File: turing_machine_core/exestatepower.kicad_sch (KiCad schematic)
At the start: 23 parts, among them J1 External Interface, U1 74LS04, U14 74LS74, U4 74LS00, U8 74LS30

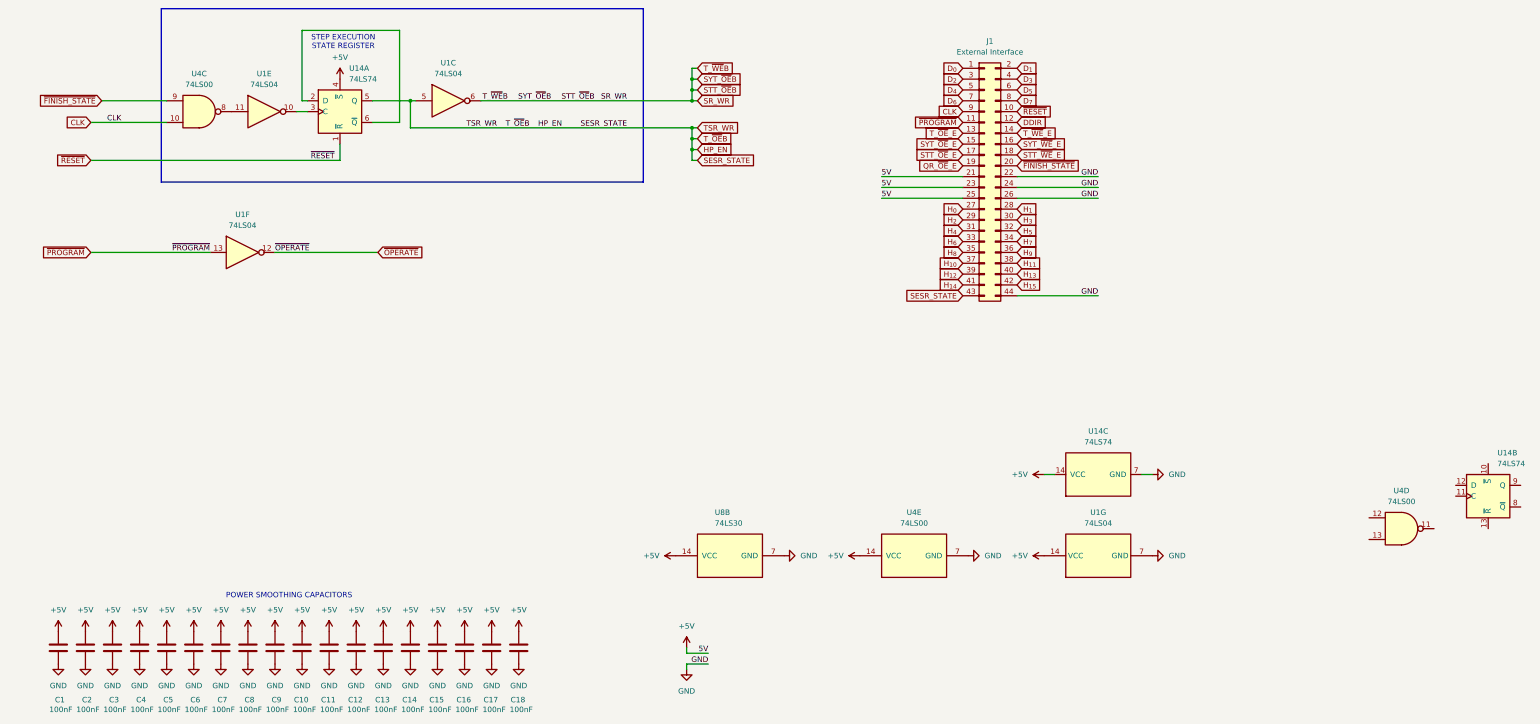
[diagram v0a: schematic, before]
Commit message: PCB layout planning and further documantation work
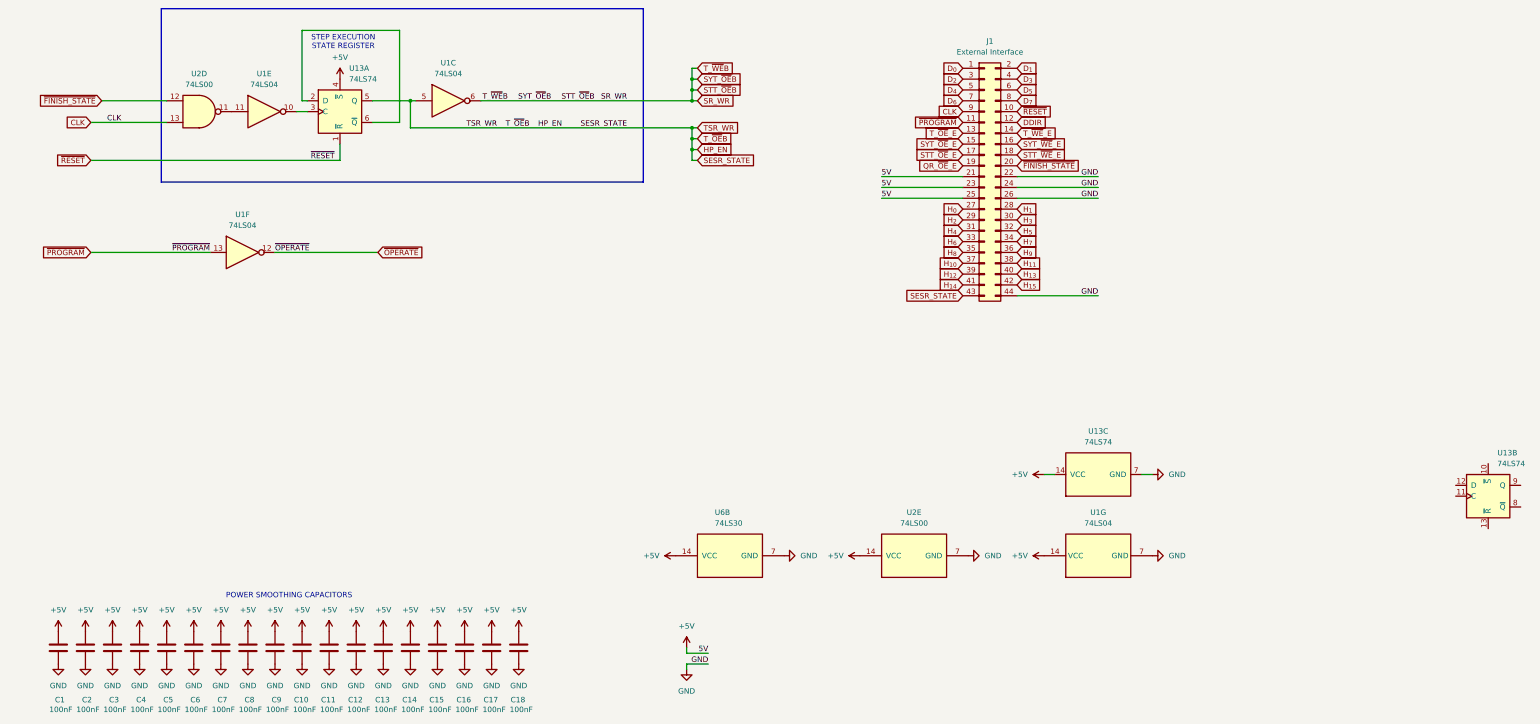
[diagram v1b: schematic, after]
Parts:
- removed U4: 74LS00, symbol 74xx:74LS00
- added U2: 74LS00, Package_DIP:DIP-14_W7.62mm, symbol 74xx:74LS00
- U1: footprint (none) -> Package_DIP:DIP-14_W7.62mm
- U13: renamed from U14; footprint (none) -> Package_DIP:DIP-14_W7.62mm
- U6: renamed from U8; footprint (none) -> Package_DIP:DIP-14_W7.62mm
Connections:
- net +5V: now also U2.14 (VCC)
- net CLK: now also U2.13
- net GND: now also U2.7 (GND)
- net ~{FINISH_STATE}: now also U2.12
- net at U1.11: now also U2.11

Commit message: finished PCB planning
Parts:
- added D1: Power LED, LED_THT:LED_D5.0mm, symbol Device:LED
- added R1: 1kΩ, Resistor_THT:R_Axial_DIN0207_L6.3mm_D2.5mm_P10.16mm_Horizontal, symbol Device:R
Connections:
- net +5V: now also U13.10 (~{S}), D1.2 (A)
- net GND: now also U13.11 (C), U13.12 (D), U13.13 (~{R}), R1.1
- new net: D1.1 (K), R1.2
- no-connect marks 0 -> 2
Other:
- moved on the sheet: U13B

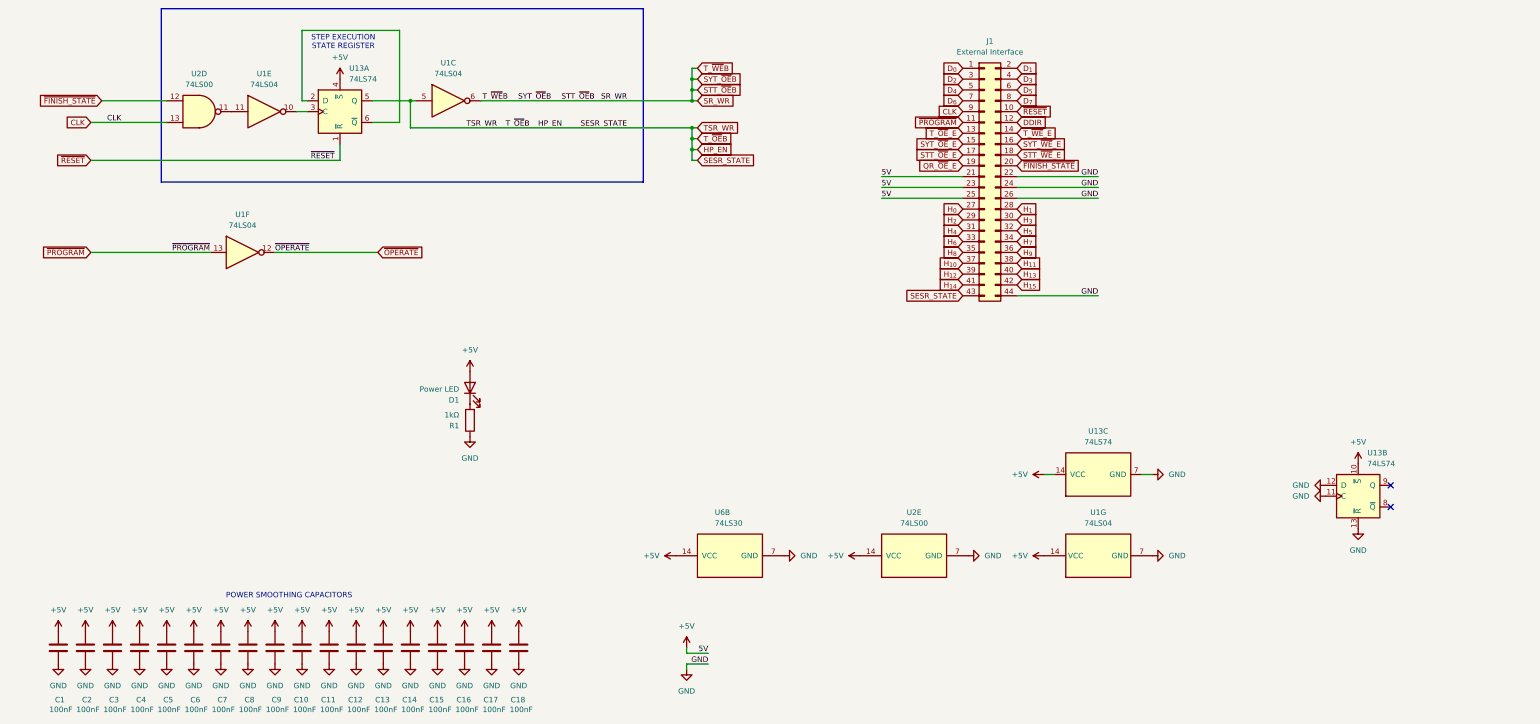
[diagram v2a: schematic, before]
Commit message: fixed schematics bugs and updated documentation
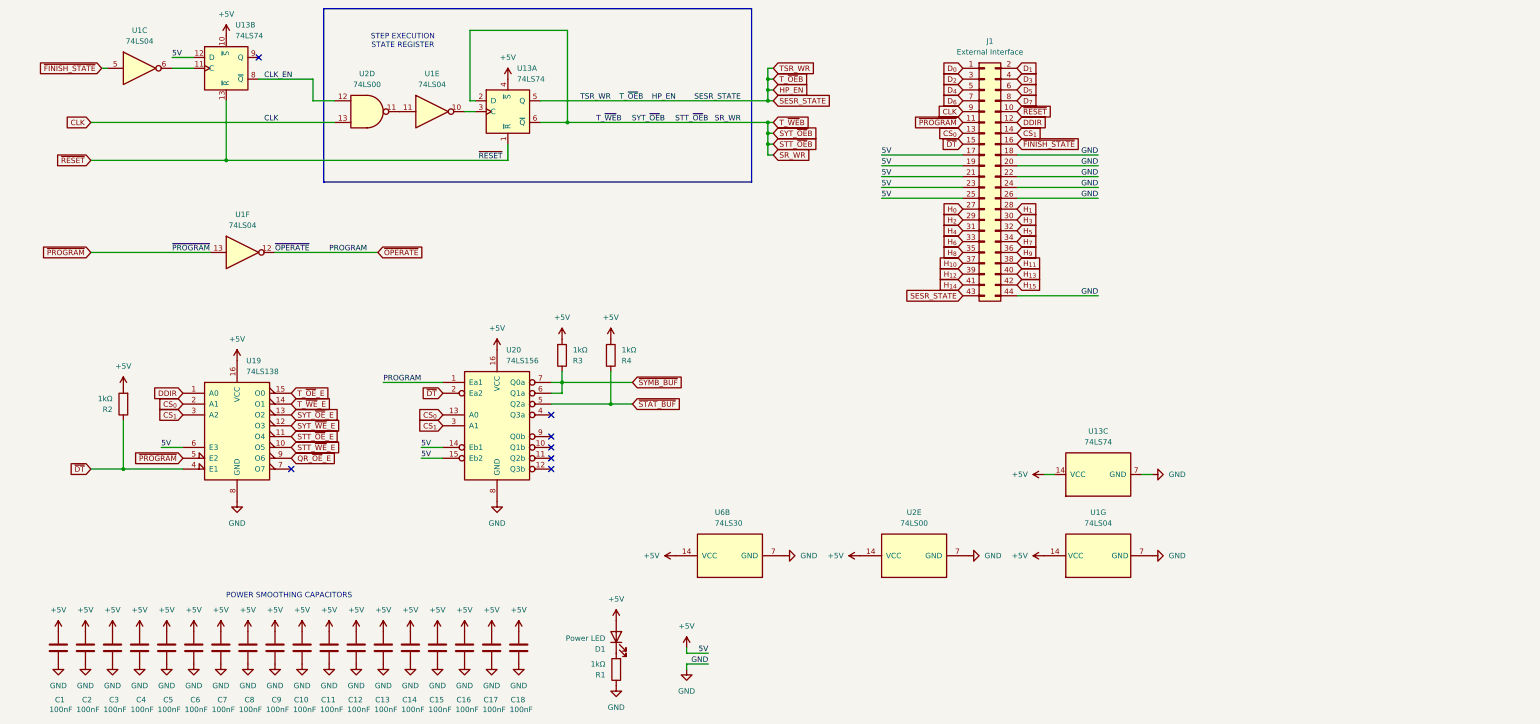
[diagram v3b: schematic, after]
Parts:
- added R2, R3, R4: 1kΩ, Resistor_THT:R_Axial_DIN0207_L6.3mm_D2.5mm_P10.16mm_Horizontal, symbol Device:R
- added U19: 74LS138, Package_DIP:DIP-16_W7.62mm, symbol 74xx:74LS138
- added U20: 74LS156, Package_DIP:DIP-16_W7.62mm, symbol 74xx:74LS156
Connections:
- net +5V: now also J1.17 (Pin_17), J1.19 (Pin_19), U13.12 (D), R2.2, R3.2, R4.2, U19.16 (VCC), U19.6 (E3), U20.14 (Eb1), U20.15 (Eb2), U20.16 (VCC)
- net DDIR: now also U19.1 (A0)
- net GND: now also J1.18 (Pin_18), J1.20 (Pin_20), U19.8 (GND), U20.8 (GND); no longer U13.11 (C), U13.12 (D), U13.13 (~{R})
- net HP_EN: no longer U1.5
- net QR_~{OE}_E: now also U19.9 (O6); no longer J1.19 (Pin_19)
- net SR_WR: now also U13.2 (D), U13.6 (~{Q}); no longer U1.6
- net STT_~{OE}_E: now also U19.11 (O4); no longer J1.17 (Pin_17)
- net STT_~{WE}_E: now also U19.10 (O5); no longer J1.18 (Pin_18)
- net SYT_~{OE}_E: now also U19.13 (O2); no longer J1.15 (Pin_15)
- net SYT_~{WE}_E: now also U19.12 (O3); no longer J1.16 (Pin_16)
- net T_~{OE}_E: now also U19.15 (O0); no longer J1.13 (Pin_13)
- net T_~{WE}_E: now also U19.14 (O1); no longer J1.14 (Pin_14)
- net ~{FINISH_STATE}: now also J1.16 (Pin_16), U1.5; no longer J1.20 (Pin_20), U2.12
- net ~{OPERATE}: now also U20.1 (Ea1)
- net ~{PROGRAM}: now also U19.5 (E2)
- net ~{RESET}: now also U13.13 (~{R})
- net CLK_EN: now reaches U13.8 (~{Q})
- net CLK_EN: now also U2.12
- new net: U1.6, U13.11 (C)
- new net CS_{0}: J1.13 (Pin_13), U19.2 (A1), U20.13 (A0)
- new net CS_{1}: J1.14 (Pin_14), U19.3 (A2), U20.3 (A1)
- new net ~{DT}: J1.15 (Pin_15), R2.1, U19.4 (E1), U20.2 (Ea2)
- new net ~{STAT_BUF}: R4.1, U20.5 (Q2a)
- new net ~{SYMB_BUF}: R3.1, U20.6 (Q1a), U20.7 (Q0a)
- no-connect marks 2 -> 7
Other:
- moved on the sheet: D1, R1, U13A, U13B, U1C, U1E, U2D

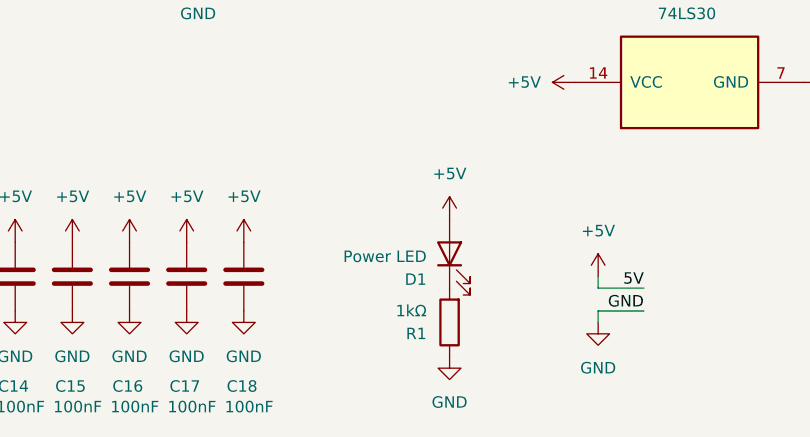
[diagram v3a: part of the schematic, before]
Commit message: adjusted PCB design for schematic fixes
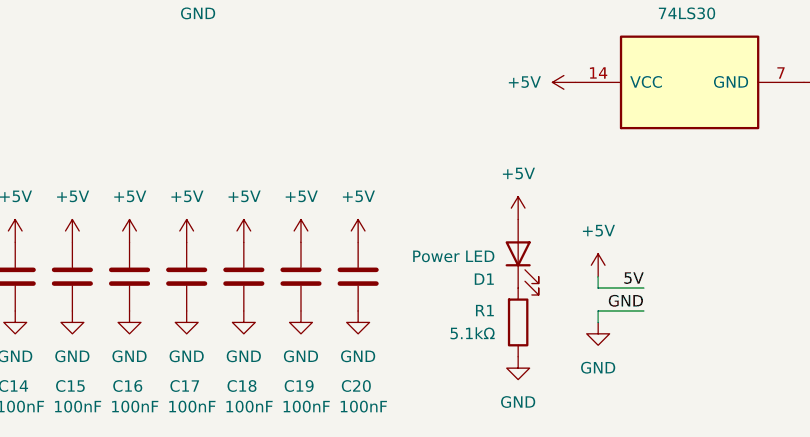
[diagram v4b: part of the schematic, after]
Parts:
- added C19, C20: 100nF, Capacitor_THT:C_Disc_D3.8mm_W2.6mm_P2.50mm, symbol Device:C
- R1: value 1kΩ -> 5.1kΩ
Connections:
- net +5V: now also C19.1, C20.1
- net GND: now also C19.2, C20.2
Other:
- moved on the sheet: D1, R1

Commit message: added edge connector to PCB
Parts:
- J1: footprint (none) -> Connector_Edge:Connector_Edge_2x22pin_odd
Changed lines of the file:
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@@
 			)
 		)
-		(property "Footprint" ""
+		(property "Footprint" "Connector_Edge:Connector_Edge_2x22pin_odd"
 			(at 234.95 69.85 0)
 			(effects

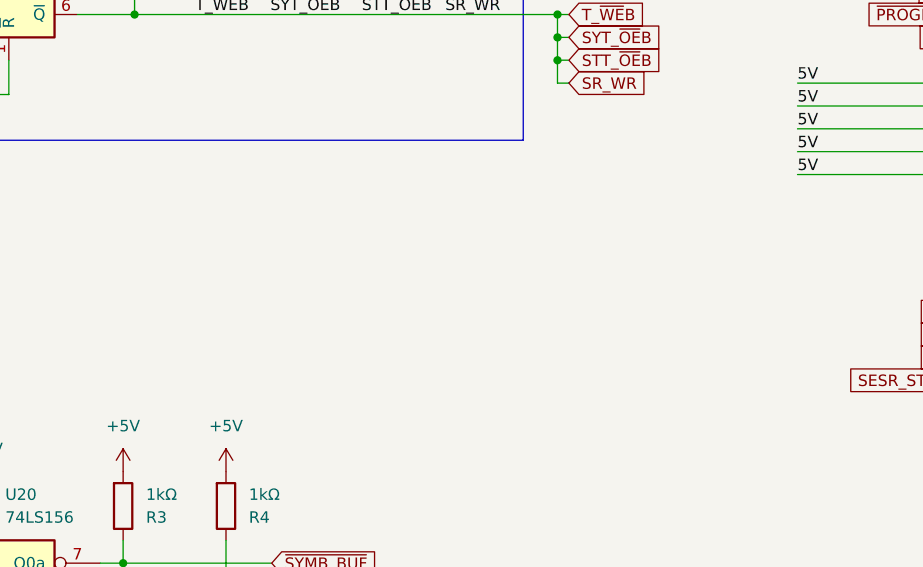
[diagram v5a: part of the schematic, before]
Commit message: added two connectors to schematics and PCB design and reformatted slightly documentation
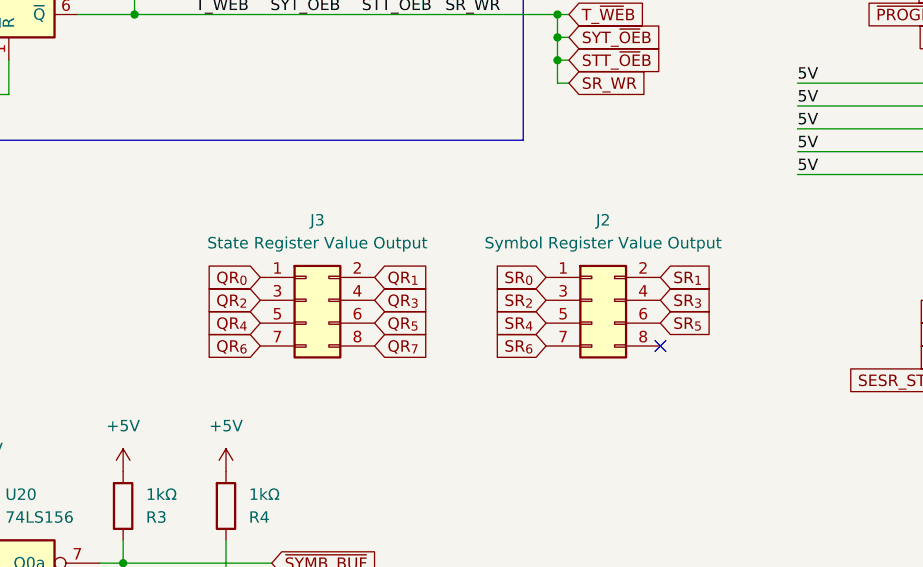
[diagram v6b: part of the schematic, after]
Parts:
- added J2: Symbol Register Value Output, Connector_PinHeader_2.54mm:PinHeader_2x04_P2.54mm_Vertical, symbol Connector_Generic:Conn_02x04_Odd_Even
- added J3: State Register Value Output, Connector_PinHeader_2.54mm:PinHeader_2x04_P2.54mm_Vertical, symbol Connector_Generic:Conn_02x04_Odd_Even
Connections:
- new net QR_{0}: J3.1 (Pin_1)
- new net QR_{1}: J3.2 (Pin_2)
- new net QR_{2}: J3.3 (Pin_3)
- new net QR_{3}: J3.4 (Pin_4)
- new net QR_{4}: J3.5 (Pin_5)
- new net QR_{5}: J3.6 (Pin_6)
- new net QR_{6}: J3.7 (Pin_7)
- new net QR_{7}: J3.8 (Pin_8)
- new net SR_{0}: J2.1 (Pin_1)
- new net SR_{1}: J2.2 (Pin_2)
- new net SR_{2}: J2.3 (Pin_3)
- new net SR_{3}: J2.4 (Pin_4)
- new net SR_{4}: J2.5 (Pin_5)
- new net SR_{5}: J2.6 (Pin_6)
- new net SR_{6}: J2.7 (Pin_7)
- no-connect marks 7 -> 8

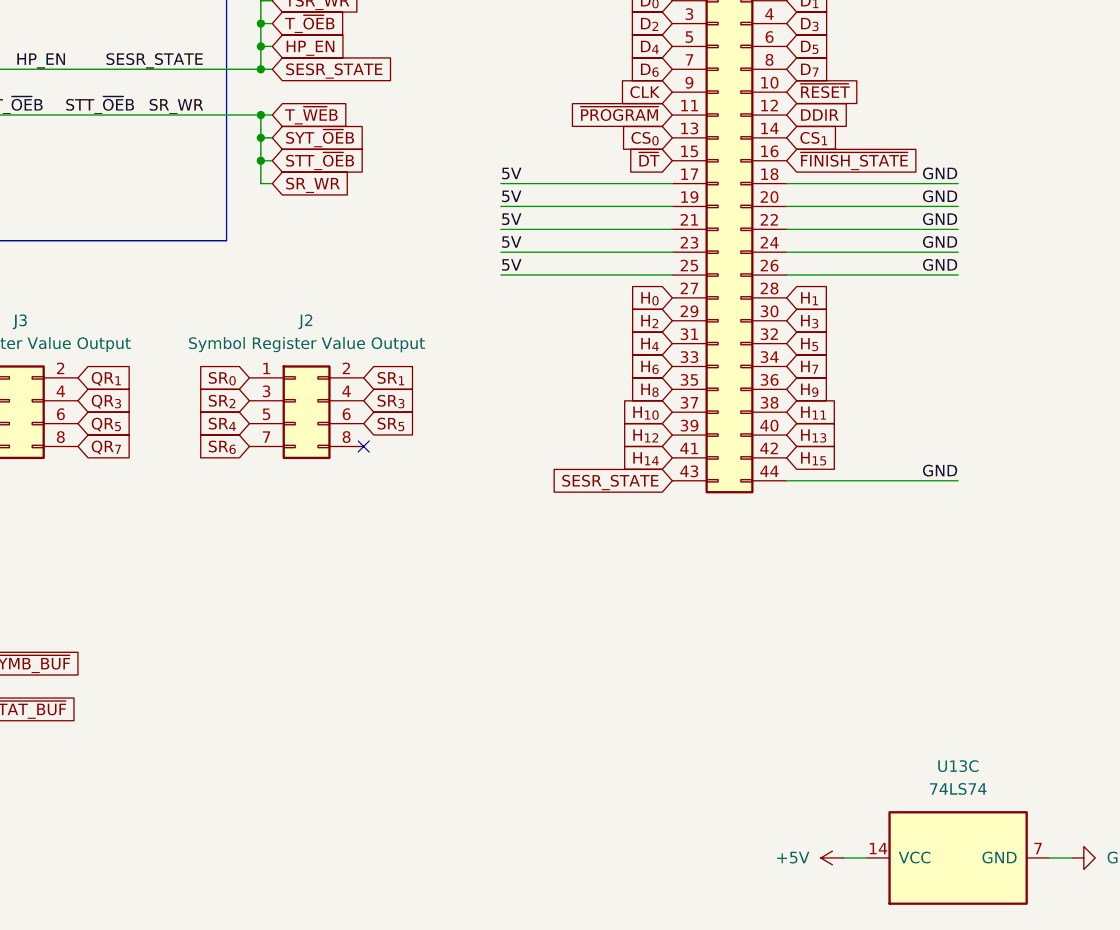
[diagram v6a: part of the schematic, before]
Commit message: moved Header Position output from main connector to dedicated one and updated documentation for that
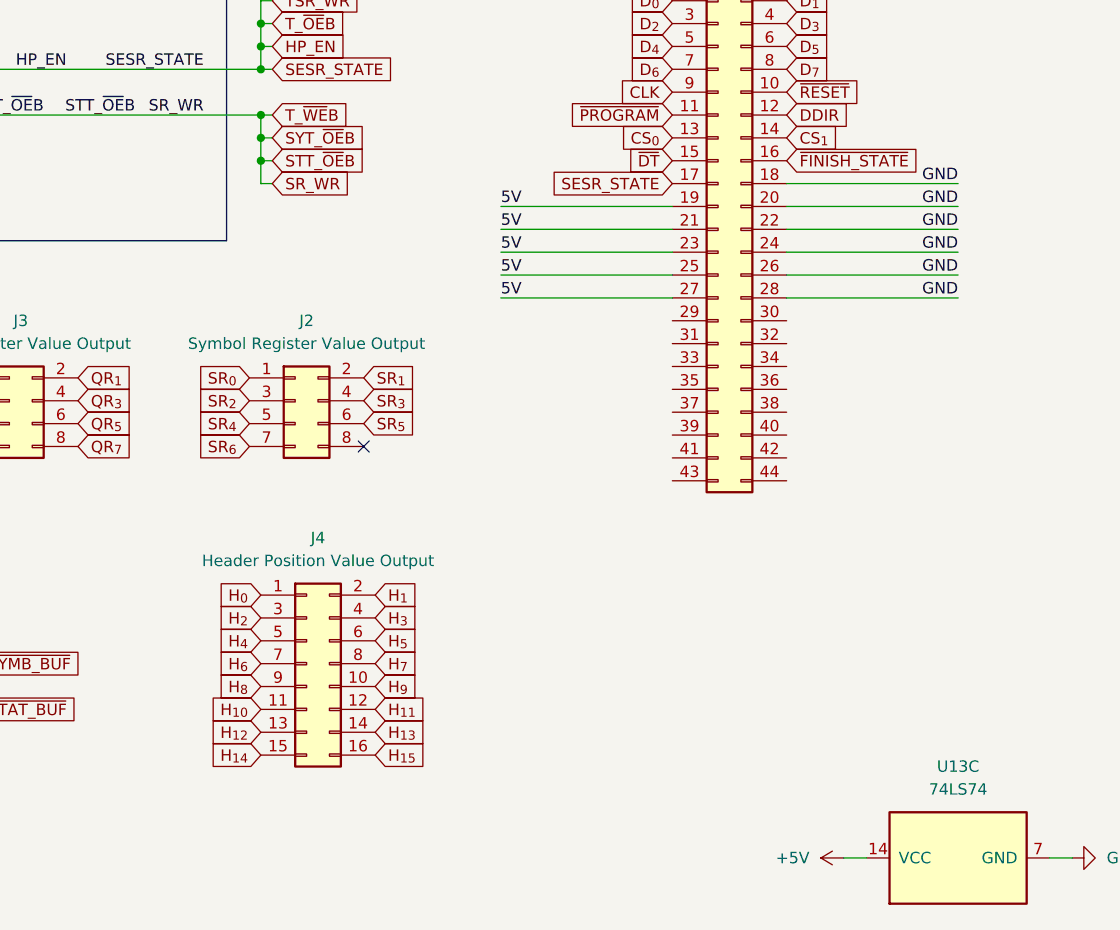
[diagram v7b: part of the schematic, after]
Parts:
- added J4: Header Position Value Output, Connector_PinHeader_2.54mm:PinHeader_2x08_P2.54mm_Vertical, symbol Connector_Generic:Conn_02x08_Odd_Even
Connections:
- net +5V: now also J1.27 (Pin_27); no longer J1.17 (Pin_17)
- net GND: now also J1.28 (Pin_28); no longer J1.44 (Pin_44)
- net HP_EN: now also J1.17 (Pin_17); no longer J1.43 (Pin_43)
- net H_{0}: now also J4.1 (Pin_1); no longer J1.27 (Pin_27)
- net H_{10}: now also J4.11 (Pin_11); no longer J1.37 (Pin_37)
- net H_{11}: now also J4.12 (Pin_12); no longer J1.38 (Pin_38)
- net H_{12}: now also J4.13 (Pin_13); no longer J1.39 (Pin_39)
- net H_{13}: now also J4.14 (Pin_14); no longer J1.40 (Pin_40)
- net H_{14}: now also J4.15 (Pin_15); no longer J1.41 (Pin_41)
- net H_{15}: now also J4.16 (Pin_16); no longer J1.42 (Pin_42)
- net H_{1}: now also J4.2 (Pin_2); no longer J1.28 (Pin_28)
- net H_{2}: now also J4.3 (Pin_3); no longer J1.29 (Pin_29)
- net H_{3}: now also J4.4 (Pin_4); no longer J1.30 (Pin_30)
- net H_{4}: now also J4.5 (Pin_5); no longer J1.31 (Pin_31)
- net H_{5}: now also J4.6 (Pin_6); no longer J1.32 (Pin_32)
- net H_{6}: now also J4.7 (Pin_7); no longer J1.33 (Pin_33)
- net H_{7}: now also J4.8 (Pin_8); no longer J1.34 (Pin_34)
- net H_{8}: now also J4.9 (Pin_9); no longer J1.35 (Pin_35)
- net H_{9}: now also J4.10 (Pin_10); no longer J1.36 (Pin_36)
